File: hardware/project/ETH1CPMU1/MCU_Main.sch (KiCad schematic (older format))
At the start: 31 parts, among them J301 Conn_02x05, J302 Conn_02x01, U301 STM32F765ZGT6, U302 24LC08, Y301 NX3225GD-8MHZ-STD-CRA-3

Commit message: Schematic design
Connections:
- net MAIN_GPIO_OUT1: now reaches U301.22 (PF10,QUADSPI_CLK,DCMI_D11,LCD_DE,EVENTOUT,ADC3_IN8)
- net MAIN_GPIO_OUT2: now reaches U301.26 (PC0,DFSDM1_CKIN0,DFSDM1_DATIN4,SAI2_FS_B,OTG_HS_ULPI_STP,FMC_SDNWE,LCD_R5,EVENTOUT,ADC1_IN10,ADC2_IN10,ADC3_IN10)
- net MAIN_STATUS_IN: now reaches U301.28 (PC2,DFSDM1_CKIN1,SPI2_MISO,DFSDM1_CKOUT,OTG_HS_ULPI_DIR,ETH_MII_TXD2,FMC_SDNE0,EVENTOUT,ADC1_IN12,ADC2_IN12,ADC3_IN12)
- net BASE_GPIO_OUT1: no longer names the net of U301.7 (PC13,EVENTOUT,RTC_TAMP2,RTC_TS,WKUP5)
- net BASE_GPIO_OUT2: no longer names the net of U301.8 (PC14,EVENTOUT,OSC32_IN)
- net BASE_MCLK renamed MAIN_MCLK
- net BASE_MISO renamed MAIN_MISO
- net BASE_MOSI renamed MAIN_MOSI
- net BASE_STATUS_IN: no longer names the net of U301.9 (PC15,EVENTOUT,OSC32_OUT)
- net BASE_~MSS renamed MAIN_~MSS
- net SPI3_MISO: no longer names the net of U301.112 (PC11,DFSDM1_DATIN5,SPI3_MISO,USART3_RX,UART4_RX,QUADSPI_BK2_NCS,SDMMC1_D3,DCMI_D4,EVENTOUT)
- net SPI3_MOSI: no longer names the net of U301.113 (PC12,TRACED3,SPI3_MOSI,I2S3_SD,USART3_CK,UART5_TX,SDMMC1_CK,DCMI_D9,EVENTOUT)
- net SPI3_SCLK: no longer names the net of U301.111 (PC10,DFSDM1_CKIN5,SPI3_SCK,I2S3_CK,USART3_TX,UART4_TX,QUADSPI_BK1_IO1,SDMMC1_D2,DCMI_D8,LCD_R2,EVENTOUT)
- no-connect marks 2 -> 5
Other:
- moved on the sheet: R301, R302, U302
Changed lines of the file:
@@
 $Descr A3 16535 11693
 encoding utf-8
-Sheet 3 12
+Sheet 3 14
 Title ""
 Date ""
@@
 Wire Wire Line
 	14600 2550 14650 2550
-Text Label 2750 6050 0    50   ~ 0
-SPI3_MOSI
-Wire Wire Line
-	3200 6050 2750 6050
-Text Label 2750 5950 0    50   ~ 0
-SPI3_MISO
-Wire Wire Line
-	3200 5950 2750 5950
-Text Label 2750 5850 0    50   ~ 0
-SPI3_SCLK
-Wire Wire Line
-	3200 5850 2750 5850
 Text Label 15050 6550 2    50   ~ 0
 TDO
@@
 L Memory_EEPROM:24LC08 U302
 U 1 1 5E082698
-P 1050 4950
-F 0 "U302" H 1250 5300 50  0000 C CNN
-F 1 "24LC08" H 1250 5200 50  0000 C CNN
-F 2 "" H 1050 4950 50  0001 C CNN
-F 3 "http://ww1.microchip.com/downloads/en/DeviceDoc/21710J.pdf" H 1050 4950 50  0001 C CNN
-	1    1050 4950
+P 1150 7100
+F 0 "U302" H 1350 7450 50  0000 C CNN
+F 1 "24LC08" H 1350 7350 50  0000 C CNN
+F 2 "" H 1150 7100 50  0001 C CNN
+F 3 "http://ww1.microchip.com/downloads/en/DeviceDoc/21710J.pdf" H 1150 7100 50  0001 C CNN
+	1    1150 7100
 	1    0    0    -1
 $EndComp
@@
 L power:+3.3V #PWR0304
 U 1 1 5E08AE5B
-P 1050 4650
-F 0 "#PWR0304" H 1050 4500 50  0001 C CNN
-F 1 "+3.3V" H 1065 4823 50  0000 C CNN
-F 2 "" H 1050 4650 50  0001 C CNN
-F 3 "" H 1050 4650 50  0001 C CNN
-	1    1050 4650
+P 1150 6800
+F 0 "#PWR0304" H 1150 6650 50  0001 C CNN
+F 1 "+3.3V" H 1165 6973 50  0000 C CNN
+F 2 "" H 1150 6800 50  0001 C CNN
+F 3 "" H 1150 6800 50  0001 C CNN
+	1    1150 6800
 	1    0    0    -1
 $EndComp
@@
 L power:GND #PWR0306
 U 1 1 5E08CDE4
-P 1050 5250
-F 0 "#PWR0306" H 1050 5000 50  0001 C CNN
-F 1 "GND" H 1055 5077 50  0000 C CNN
-F 2 "" H 1050 5250 50  0001 C CNN
-F 3 "" H 1050 5250 50  0001 C CNN
-	1    1050 5250
-	1    0    0    -1
-$EndComp
-Wire Wire Line
-	650  4850 600  4850
-Wire Wire Line
-	600  4850 600  4950
-Wire Wire Line
-	600  5050 650  5050
+P 1150 7400
+F 0 "#PWR0306" H 1150 7150 50  0001 C CNN
+F 1 "GND" H 1155 7227 50  0000 C CNN
+F 2 "" H 1150 7400 50  0001 C CNN
+F 3 "" H 1150 7400 50  0001 C CNN
+	1    1150 7400
+	1    0    0    -1
+$EndComp
+Wire Wire Line
+	750  7000 700  7000
+Wire Wire Line
+	700  7000 700  7100
+Wire Wire Line
+	700  7200 750  7200
 $Comp
 L power:GND #PWR0305
 U 1 1 5E096BB8
-P 600 5250
-F 0 "#PWR0305" H 600 5000 50  0001 C CNN
-F 1 "GND" H 605 5077 50  0000 C CNN
-F 2 "" H 600 5250 50  0001 C CNN
-F 3 "" H 600 5250 50  0001 C CNN
-	1    600  5250
-	1    0    0    -1
-$EndComp
-Wire Wire Line
-	600  5250 600  5050
-Connection ~ 600  5050
-Wire Wire Line
-	650  4950 600  4950
-Connection ~ 600  4950
-Wire Wire Line
-	600  4950 600  5050
-Wire Wire Line
-	1450 5050 1950 5050
-Text Label 1950 5050 2    50   ~ 0
+P 700 7400
+F 0 "#PWR0305" H 700 7150 50  0001 C CNN
+F 1 "GND" H 705 7227 50  0000 C CNN
+F 2 "" H 700 7400 50  0001 C CNN
+F 3 "" H 700 7400 50  0001 C CNN
+	1    700  7400
+	1    0    0    -1
+$EndComp
+Wire Wire Line
+	700  7400 700  7200
+Connection ~ 700  7200
+Wire Wire Line
+	750  7100 700  7100
+Connection ~ 700  7100
+Wire Wire Line
+	700  7100 700  7200
+Wire Wire Line
+	1550 7200 2050 7200
+Text Label 2050 7200 2    50   ~ 0
 EEPROM_WP
-Text Label 1950 4950 2    50   ~ 0
+Text Label 2050 7100 2    50   ~ 0
 EEPROM_SCL
-Text Label 1950 4850 2    50   ~ 0
+Text Label 2050 7000 2    50   ~ 0
 EEPROM_SDA
 $Comp
 L Device:R R301
 U 1 1 5E0F3906
-P 2000 4650
-F 0 "R301" H 2070 4696 50  0000 L CNN
-F 1 "4k7" H 2070 4605 50  0000 L CNN
-F 2 "Resistor_SMD:R_0603_1608Metric_Pad1.05x0.95mm_HandSolder" V 1930 4650 50  0001 C CNN
-F 3 "~" H 2000 4650 50  0001 C CNN
-	1    2000 4650
+P 2100 6800
+F 0 "R301" H 2170 6846 50  0000 L CNN
+F 1 "4k7" H 2170 6755 50  0000 L CNN
+F 2 "Resistor_SMD:R_0603_1608Metric_Pad1.05x0.95mm_HandSolder" V 2030 6800 50  0001 C CNN
+F 3 "~" H 2100 6800 50  0001 C CNN
+	1    2100 6800
 	1    0    0    -1
 $EndComp
@@
 L Device:R R302
 U 1 1 5E0F3C03
-P 2350 4650
-F 0 "R302" H 2420 4696 50  0000 L CNN
-F 1 "4k7" H 2420 4605 50  0000 L CNN
-F 2 "Resistor_SMD:R_0603_1608Metric_Pad1.05x0.95mm_HandSolder" V 2280 4650 50  0001 C CNN
-F 3 "~" H 2350 4650 50  0001 C CNN
-	1    2350 4650
-	1    0    0    -1
-$EndComp
-Wire Wire Line
-	2000 4850 2000 4800
-Wire Wire Line
-	1450 4850 2000 4850
-Wire Wire Line
-	2350 4950 2350 4800
-Wire Wire Line
-	1450 4950 2350 4950
-Wire Wire Line
-	2000 4500 2000 4450
-Wire Wire Line
-	2000 4450 2350 4450
-Wire Wire Line
-	2350 4450 2350 4500
+P 2450 6800
+F 0 "R302" H 2520 6846 50  0000 L CNN
+F 1 "4k7" H 2520 6755 50  0000 L CNN
+F 2 "Resistor_SMD:R_0603_1608Metric_Pad1.05x0.95mm_HandSolder" V 2380 6800 50  0001 C CNN
+F 3 "~" H 2450 6800 50  0001 C CNN
+	1    2450 6800
+	1    0    0    -1
+$EndComp
+Wire Wire Line
+	2100 7000 2100 6950
+Wire Wire Line
+	1550 7000 2100 7000
+Wire Wire Line
+	2450 7100 2450 6950
+Wire Wire Line
+	1550 7100 2450 7100
+Wire Wire Line
+	2100 6650 2100 6600
+Wire Wire Line
+	2100 6600 2450 6600
+Wire Wire Line
+	2450 6600 2450 6650
 $Comp
 L power:+3.3V #PWR0303
 U 1 1 5E117FC1
-P 2350 4400
-F 0 "#PWR0303" H 2350 4250 50  0001 C CNN
-F 1 "+3.3V" H 2365 4573 50  0000 C CNN
-F 2 "" H 2350 4400 50  0001 C CNN
-F 3 "" H 2350 4400 50  0001 C CNN
-	1    2350 4400
-	1    0    0    -1
-$EndComp
-Wire Wire Line
-	2350 4400 2350 4450
-Connection ~ 2350 4450
+P 2450 6550
+F 0 "#PWR0303" H 2450 6400 50  0001 C CNN
+F 1 "+3.3V" H 2465 6723 50  0000 C CNN
+F 2 "" H 2450 6550 50  0001 C CNN
+F 3 "" H 2450 6550 50  0001 C CNN
+	1    2450 6550
+	1    0    0    -1
+$EndComp
+Wire Wire Line
+	2450 6550 2450 6600
+Connection ~ 2450 6600
 Wire Wire Line
 	3200 2750 2700 2750
@@
 Wire Wire Line
 	700  9650 700  9550
-Text HLabel 3150 2150 0    50   Output ~ 0
-BASE_MCLK
-Text HLabel 3150 2350 0    50   Output ~ 0
-BASE_MOSI
-Text HLabel 3150 2250 0    50   Input ~ 0
-BASE_MISO
-Text HLabel 3150 2050 0    50   Output ~ 0
-BASE_~MSS
-Wire Wire Line
-	3150 2350 3200 2350
-Wire Wire Line
-	3200 2250 3150 2250
-Wire Wire Line
-	3150 2150 3200 2150
-Wire Wire Line
-	3200 2050 3150 2050
 Text HLabel 14650 7550 2    50   Output ~ 0
 TRIG_EN
@@
 Wire Wire Line
 	14600 7750 14650 7750
-Text HLabel 3150 6350 0    50   Input ~ 0
-BASE_STATUS_IN
-Text HLabel 3150 6250 0    50   Output ~ 0
-BASE_GPIO_OUT2
-Text HLabel 3150 6150 0    50   Output ~ 0
-BASE_GPIO_OUT1
-Wire Wire Line
-	3150 6150 3200 6150
-Wire Wire Line
-	3200 6250 3150 6250
-Wire Wire Line
-	3150 6350 3200 6350
+Text HLabel 3150 5050 0    50   Input ~ 0
+MAIN_STATUS_IN
+Text HLabel 3150 4850 0    50   Output ~ 0
+MAIN_GPIO_OUT2
+Text HLabel 3150 2450 0    50   Output ~ 0
+MAIN_GPIO_OUT1
+Wire Wire Line
+	3150 2450 3200 2450
+Wire Wire Line
+	3200 4850 3150 4850
+Wire Wire Line
+	3150 5050 3200 5050
+Wire Wire Line
+	3200 2050 3150 2050
+Wire Wire Line
+	3150 2150 3200 2150
+Wire Wire Line
+	3200 2250 3150 2250
+Wire Wire Line
+	3150 2350 3200 2350
+Text HLabel 3150 2050 0    50   Output ~ 0
+MAIN_~MSS
+Text HLabel 3150 2250 0    50   Input ~ 0
+MAIN_MISO
+Text HLabel 3150 2350 0    50   Output ~ 0
+MAIN_MOSI
+Text HLabel 3150 2150 0    50   Output ~ 0
+MAIN_MCLK
+NoConn ~ 3200 5850
+NoConn ~ 3200 5950
+NoConn ~ 3200 6050
 $EndSCHEMATC

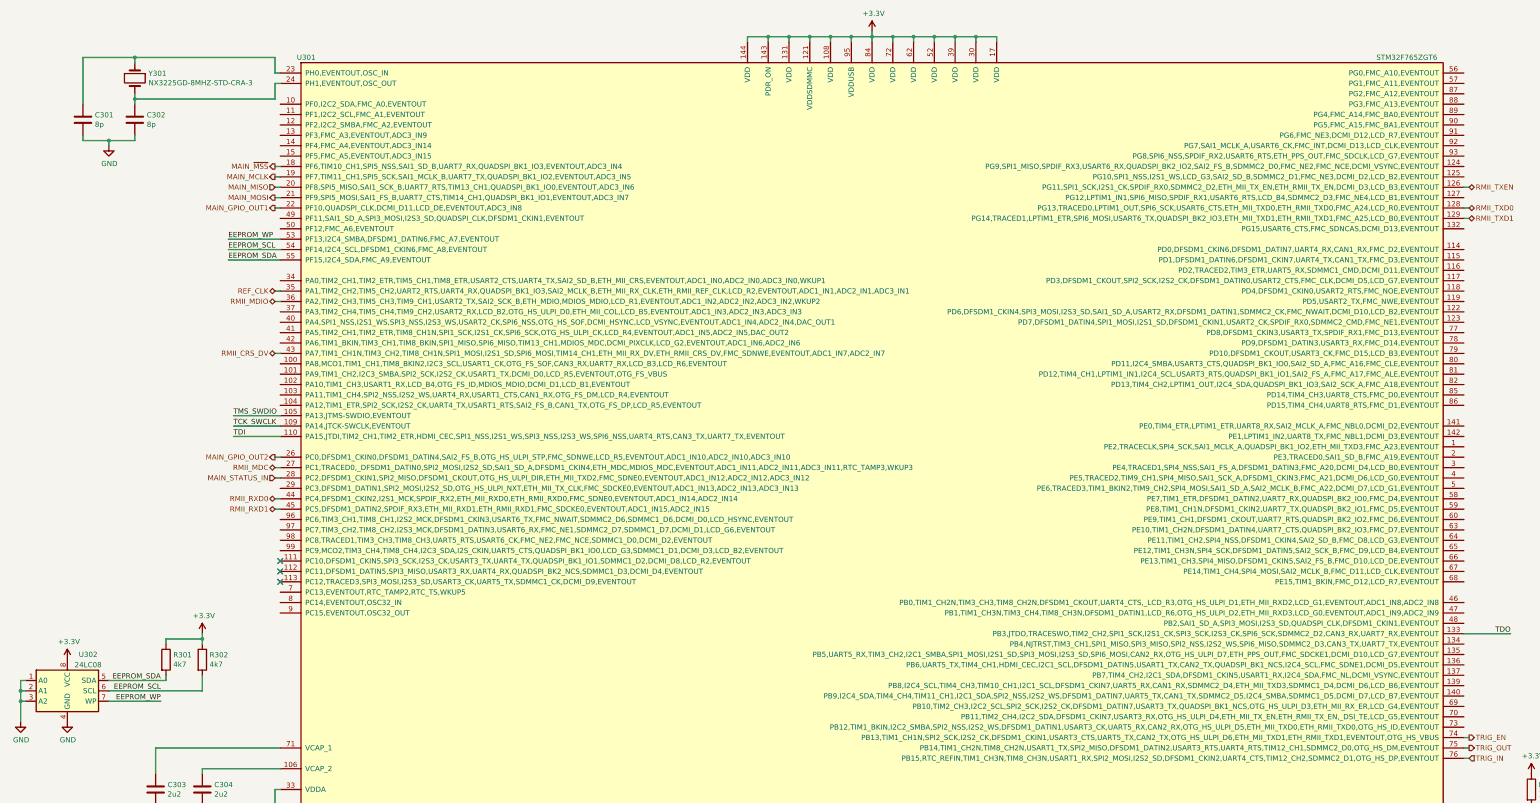
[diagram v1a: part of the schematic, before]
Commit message: Function generator schematic design.
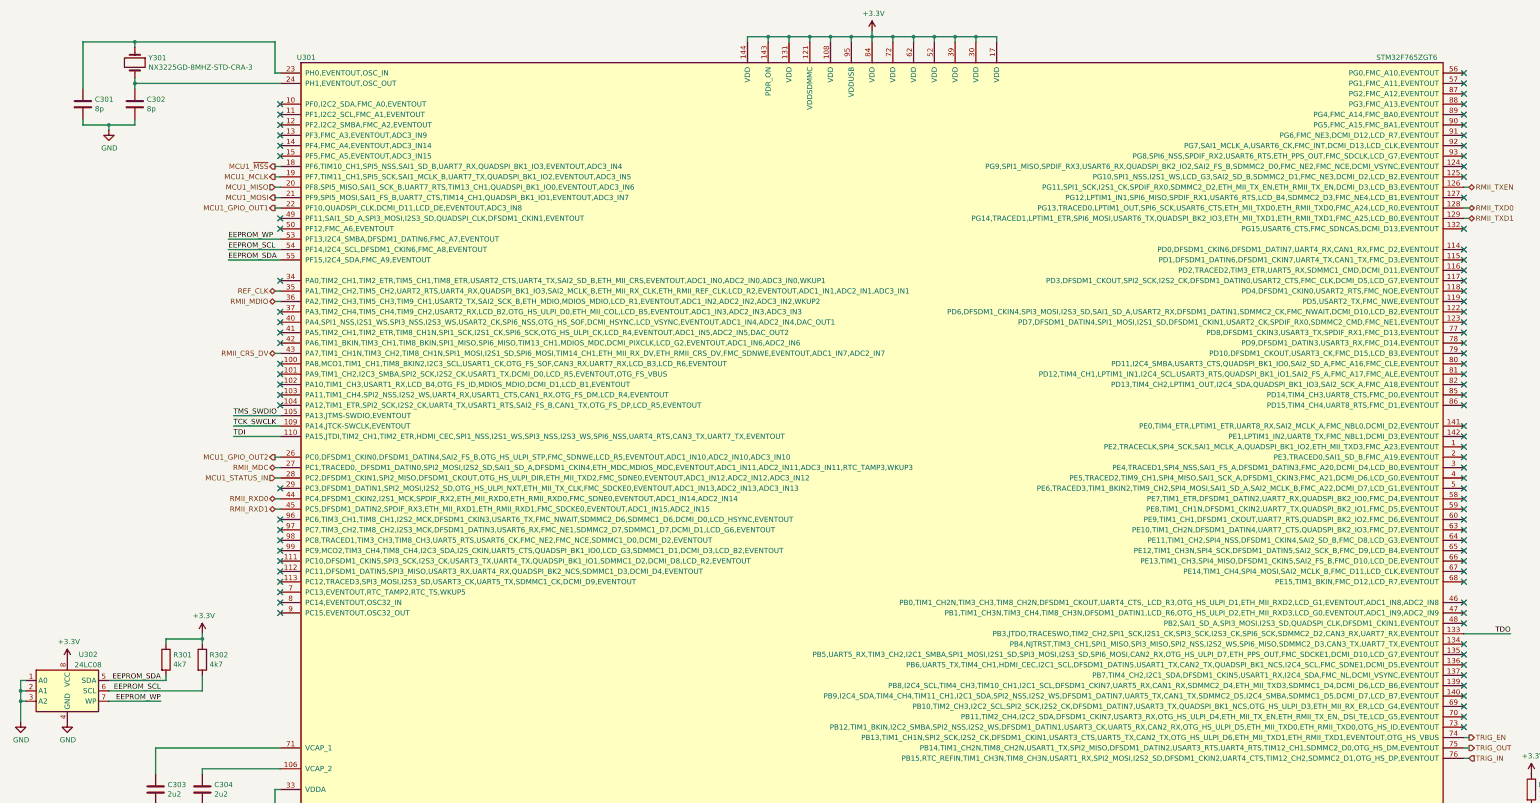
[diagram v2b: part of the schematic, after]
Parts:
- C303, C304: footprint (none) -> Capacitor_SMD:C_0805_2012Metric_Pad1.15x1.40mm_HandSolder
- C306, C320: footprint (none) -> Capacitor_SMD:C_0603_1608Metric_Pad1.05x0.95mm_HandSolder
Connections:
- net MAIN_GPIO_OUT1 renamed MCU1_GPIO_OUT1
- net MAIN_GPIO_OUT2 renamed MCU1_GPIO_OUT2
- net MAIN_MCLK renamed MCU1_MCLK
- net MAIN_MISO renamed MCU1_MISO
- net MAIN_MOSI renamed MCU1_MOSI
- net MAIN_STATUS_IN renamed MCU1_STATUS_IN
- net MAIN_~MSS renamed MCU1_~MSS
- no-connect marks 5 -> 88
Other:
- moved on the sheet: C301, C302, Y301
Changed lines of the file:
@@
 $Descr A3 16535 11693
 encoding utf-8
-Sheet 3 14
+Sheet 3 15
 Title ""
 Date ""
@@
 F 0 "C306" H 3265 8946 50  0000 L CNN
 F 1 "1u" H 3265 8855 50  0000 L CNN
-F 2 "" H 3188 8750 50  0001 C CNN
+F 2 "Capacitor_SMD:C_0603_1608Metric_Pad1.05x0.95mm_HandSolder" H 3188 8750 50  0001 C CNN
 F 3 "~" H 3150 8900 50  0001 C CNN
 	1    3150 8900
@@
 F 0 "C320" H 7365 10746 50  0000 L CNN
 F 1 "1u" H 7365 10655 50  0000 L CNN
-F 2 "" H 7288 10550 50  0001 C CNN
+F 2 "Capacitor_SMD:C_0603_1608Metric_Pad1.05x0.95mm_HandSolder" H 7288 10550 50  0001 C CNN
 F 3 "~" H 7250 10700 50  0001 C CNN
 	1    7250 10700
@@
 F 0 "C304" H 2565 8096 50  0000 L CNN
 F 1 "2u2" H 2565 8005 50  0000 L CNN
-F 2 "" H 2488 7900 50  0001 C CNN
+F 2 "Capacitor_SMD:C_0805_2012Metric_Pad1.15x1.40mm_HandSolder" H 2488 7900 50  0001 C CNN
 F 3 "~" H 2450 8050 50  0001 C CNN
 	1    2450 8050
@@
 F 0 "C303" H 2115 8096 50  0000 L CNN
 F 1 "2u2" H 2115 8005 50  0000 L CNN
-F 2 "" H 2038 7900 50  0001 C CNN
+F 2 "Capacitor_SMD:C_0805_2012Metric_Pad1.15x1.40mm_HandSolder" H 2038 7900 50  0001 C CNN
 F 3 "~" H 2000 8050 50  0001 C CNN
 	1    2000 8050
@@
 L Device:Crystal Y301
 U 1 1 5DBCE9A3
-P 1800 1200
-F 0 "Y301" V 1754 1331 50  0000 L CNN
-F 1 "NX3225GD-8MHZ-STD-CRA-3" V 1845 1331 50  0000 L CNN
-F 2 "" H 1800 1200 50  0001 C CNN
-F 3 "~" H 1800 1200 50  0001 C CNN
-	1    1800 1200
+P 1800 1050
+F 0 "Y301" V 1754 1181 50  0000 L CNN
+F 1 "NX3225GD-8MHZ-STD-CRA-3" V 1845 1181 50  0000 L CNN
+F 2 "" H 1800 1050 50  0001 C CNN
+F 3 "~" H 1800 1050 50  0001 C CNN
+	1    1800 1050
 	0    1    1    0
 $EndComp
 Wire Wire Line
-	3200 1250 3150 1250
-Wire Wire Line
-	3150 1250 3150 1400
-Wire Wire Line
-	3150 1400 1800 1400
-Wire Wire Line
-	1800 1400 1800 1350
-Wire Wire Line
-	1800 1050 1800 1000
-Wire Wire Line
-	1800 1000 3150 1000
-Wire Wire Line
-	3150 1000 3150 1150
+	1800 1250 1800 1200
+Wire Wire Line
+	1800 900  1800 850
+Wire Wire Line
+	1800 850  3150 850
+Wire Wire Line
+	3150 850  3150 1150
 Wire Wire Line
 	3150 1150 3200 1150
@@
 L Device:C C302
 U 1 1 5DBE0849
-P 1800 1600
-F 0 "C302" H 1915 1646 50  0000 L CNN
-F 1 "8p" H 1915 1555 50  0000 L CNN
-F 2 "Capacitor_SMD:C_0603_1608Metric_Pad1.05x0.95mm_HandSolder" H 1838 1450 50  0001 C CNN
-F 3 "~" H 1800 1600 50  0001 C CNN
-	1    1800 1600
+P 1800 1450
+F 0 "C302" H 1915 1496 50  0000 L CNN
+F 1 "8p" H 1915 1405 50  0000 L CNN
+F 2 "Capacitor_SMD:C_0603_1608Metric_Pad1.05x0.95mm_HandSolder" H 1838 1300 50  0001 C CNN
+F 3 "~" H 1800 1450 50  0001 C CNN
+	1    1800 1450
 	1    0    0    -1
 $EndComp
@@
 L Device:C C301
 U 1 1 5DBE0C2D
-P 1300 1600
-F 0 "C301" H 1415 1646 50  0000 L CNN
-F 1 "8p" H 1415 1555 50  0000 L CNN
-F 2 "Capacitor_SMD:C_0603_1608Metric_Pad1.05x0.95mm_HandSolder" H 1338 1450 50  0001 C CNN
-F 3 "~" H 1300 1600 50  0001 C CNN
-	1    1300 1600
-	1    0    0    -1
-$EndComp
-Wire Wire Line
-	1800 1450 1800 1400
-Connection ~ 1800 1400
-Wire Wire Line
-	1800 1000 1300 1000
-Wire Wire Line
-	1300 1000 1300 1450
-Connection ~ 1800 1000
-Wire Wire Line
-	1300 1750 1300 1800
-Wire Wire Line
-	1300 1800 1550 1800
-Wire Wire Line
-	1800 1800 1800 1750
+P 1300 1450
+F 0 "C301" H 1415 1496 50  0000 L CNN
+F 1 "8p" H 1415 1405 50  0000 L CNN
+F 2 "Capacitor_SMD:C_0603_1608Metric_Pad1.05x0.95mm_HandSolder" H 1338 1300 50  0001 C CNN
+F 3 "~" H 1300 1450 50  0001 C CNN
+	1    1300 1450
+	1    0    0    -1
+$EndComp
+Wire Wire Line
+	1800 1300 1800 1250
+Connection ~ 1800 1250
+Wire Wire Line
+	1800 850  1300 850
+Wire Wire Line
+	1300 850  1300 1300
+Connection ~ 1800 850
+Wire Wire Line
+	1300 1600 1300 1650
+Wire Wire Line
+	1300 1650 1550 1650
+Wire Wire Line
+	1800 1650 1800 1600
 $Comp
 L power:GND #PWR0302
 U 1 1 5DC11C96
-P 1550 1850
-F 0 "#PWR0302" H 1550 1600 50  0001 C CNN
-F 1 "GND" H 1555 1677 50  0000 C CNN
-F 2 "" H 1550 1850 50  0001 C CNN
-F 3 "" H 1550 1850 50  0001 C CNN
-	1    1550 1850
-	1    0    0    -1
-$EndComp
-Wire Wire Line
-	1550 1850 1550 1800
-Connection ~ 1550 1800
-Wire Wire Line
-	1550 1800 1800 1800
+P 1550 1700
+F 0 "#PWR0302" H 1550 1450 50  0001 C CNN
+F 1 "GND" H 1555 1527 50  0000 C CNN
+F 2 "" H 1550 1700 50  0001 C CNN
+F 3 "" H 1550 1700 50  0001 C CNN
+	1    1550 1700
+	1    0    0    -1
+$EndComp
+Wire Wire Line
+	1550 1700 1550 1650
+Connection ~ 1550 1650
+Wire Wire Line
+	1550 1650 1800 1650
 Wire Wire Line
 	3200 4450 2750 4450
@@
 	14600 7750 14650 7750
 Text HLabel 3150 5050 0    50   Input ~ 0
-MAIN_STATUS_IN
+MCU1_STATUS_IN
 Text HLabel 3150 4850 0    50   Output ~ 0
-MAIN_GPIO_OUT2
+MCU1_GPIO_OUT2
 Text HLabel 3150 2450 0    50   Output ~ 0
-MAIN_GPIO_OUT1
+MCU1_GPIO_OUT1
 Wire Wire Line
 	3150 2450 3200 2450
@@
 	3150 2350 3200 2350
 Text HLabel 3150 2050 0    50   Output ~ 0
-MAIN_~MSS
+MCU1_~MSS
 Text HLabel 3150 2250 0    50   Input ~ 0
-MAIN_MISO
+MCU1_MISO
 Text HLabel 3150 2350 0    50   Output ~ 0
-MAIN_MOSI
+MCU1_MOSI
 Text HLabel 3150 2150 0    50   Output ~ 0
-MAIN_MCLK
+MCU1_MCLK
 NoConn ~ 3200 5850
 NoConn ~ 3200 5950
 NoConn ~ 3200 6050
+Wire Wire Line
+	1800 1250 3200 1250
+NoConn ~ 3200 1750
+NoConn ~ 3200 1850
+NoConn ~ 3200 1950
+NoConn ~ 3200 2550
+NoConn ~ 3200 2650
+NoConn ~ 3200 3150
+NoConn ~ 3200 1450
+NoConn ~ 3200 1550
+NoConn ~ 3200 1650
+NoConn ~ 3200 3450
+NoConn ~ 3200 3550
+NoConn ~ 3200 3650
+NoConn ~ 3200 3750
+NoConn ~ 3200 3950
+NoConn ~ 3200 4050
+NoConn ~ 3200 4150
+NoConn ~ 3200 4250
+NoConn ~ 3200 4350
+NoConn ~ 3200 5150
+NoConn ~ 3200 5450
+NoConn ~ 3200 5550
+NoConn ~ 3200 5650
+NoConn ~ 3200 5750
+NoConn ~ 3200 6150
+NoConn ~ 3200 6250
+NoConn ~ 3200 6350
+NoConn ~ 14600 1150
+NoConn ~ 14600 1250
+NoConn ~ 14600 1350
+NoConn ~ 14600 1450
+NoConn ~ 14600 1550
+NoConn ~ 14600 1650
+NoConn ~ 14600 1750
+NoConn ~ 14600 1850
+NoConn ~ 14600 1950
+NoConn ~ 14600 2050
+NoConn ~ 14600 2150
+NoConn ~ 14600 2350
+NoConn ~ 14600 2650
+NoConn ~ 14600 2850
+NoConn ~ 14600 2950
+NoConn ~ 14600 3050
+NoConn ~ 14600 3150
+NoConn ~ 14600 3250
+NoConn ~ 14600 3350
+NoConn ~ 14600 3450
+NoConn ~ 14600 3550
+NoConn ~ 14600 3650
+NoConn ~ 14600 3750
+NoConn ~ 14600 3850
+NoConn ~ 14600 3950
+NoConn ~ 14600 4050
+NoConn ~ 14600 4150
+NoConn ~ 14600 4250
+NoConn ~ 14600 4350
+NoConn ~ 14600 4550
+NoConn ~ 14600 4650
+NoConn ~ 14600 4750
+NoConn ~ 14600 4850
+NoConn ~ 14600 4950
+NoConn ~ 14600 5050
+NoConn ~ 14600 5150
+NoConn ~ 14600 5250
+NoConn ~ 14600 5350
+NoConn ~ 14600 5450
+NoConn ~ 14600 5550
+NoConn ~ 14600 5650
+NoConn ~ 14600 5750
+NoConn ~ 14600 5850
+NoConn ~ 14600 5950
+NoConn ~ 14600 6050
+NoConn ~ 14600 6250
+NoConn ~ 14600 6350
+NoConn ~ 14600 6450
+NoConn ~ 14600 6650
+NoConn ~ 14600 6750
+NoConn ~ 14600 6850
+NoConn ~ 14600 6950
+NoConn ~ 14600 7050
+NoConn ~ 14600 7150
+NoConn ~ 14600 7250
+NoConn ~ 14600 7350
+NoConn ~ 14600 7450
 $EndSCHEMATC

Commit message: New footprint development, changes in schematics.
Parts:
- FB301: footprint Resistor_SMD:R_0805_2012Metric_Pad1.15x1.40mm_HandSolder -> Inductor_SMD:L_0805_2012Metric_Pad1.15x1.40mm_HandSolder
- J301: footprint (none) -> Connector_PinHeader_1.27mm:PinHeader_2x05_P1.27mm_Vertical
- J302: footprint (none) -> Connector_PinHeader_2.54mm:PinHeader_1x02_P2.54mm_Vertical
- Y301: footprint (none) -> ETH1CPMU1:NX3225GD
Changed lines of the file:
@@
 F 0 "J301" H 9900 10867 50  0000 C CNN
 F 1 "Conn_02x05" H 9900 10776 50  0000 C CNN
-F 2 "" H 9850 10450 50  0001 C CNN
+F 2 "Connector_PinHeader_1.27mm:PinHeader_2x05_P1.27mm_Vertical" H 9850 10450 50  0001 C CNN
 F 3 "~" H 9850 10450 50  0001 C CNN
 	1    9850 10450
@@
 F 0 "FB301" V 6726 10500 50  0000 C CNN
 F 1 "742792031" V 6817 10500 50  0000 C CNN
-F 2 "Resistor_SMD:R_0805_2012Metric_Pad1.15x1.40mm_HandSolder" V 6930 10500 50  0001 C CNN
+F 2 "Inductor_SMD:L_0805_2012Metric_Pad1.15x1.40mm_HandSolder" V 6930 10500 50  0001 C CNN
 F 3 "~" H 7000 10500 50  0001 C CNN
 	1    7000 10500
@@
 F 0 "J302" V 8054 10730 50  0000 L CNN
 F 1 "Conn_02x01" V 8145 10730 50  0000 L CNN
-F 2 "" H 8050 10650 50  0001 C CNN
+F 2 "Connector_PinHeader_2.54mm:PinHeader_1x02_P2.54mm_Vertical" H 8050 10650 50  0001 C CNN
 F 3 "~" H 8050 10650 50  0001 C CNN
 	1    8050 10650
@@
 F 0 "Y301" V 1754 1181 50  0000 L CNN
 F 1 "NX3225GD-8MHZ-STD-CRA-3" V 1845 1181 50  0000 L CNN
-F 2 "" H 1800 1050 50  0001 C CNN
+F 2 "ETH1CPMU1:NX3225GD" H 1800 1050 50  0001 C CNN
 F 3 "~" H 1800 1050 50  0001 C CNN
 	1    1800 1050

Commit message: Schematic and PCB design.
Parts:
- U302: value 24LC08 -> 24LC08B-E/MS; footprint (none) -> Package_SO:MSOP-8_3x3mm_P0.65mm
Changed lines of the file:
@@
 U 1 1 5E082698
 P 1150 7100
-F 0 "U302" H 1350 7450 50  0000 C CNN
-F 1 "24LC08" H 1350 7350 50  0000 C CNN
-F 2 "" H 1150 7100 50  0001 C CNN
+F 0 "U302" H 1500 7450 50  0000 C CNN
+F 1 "24LC08B-E/MS" H 1500 7350 50  0000 C CNN
+F 2 "Package_SO:MSOP-8_3x3mm_P0.65mm" H 1150 7100 50  0001 C CNN
 F 3 "http://ww1.microchip.com/downloads/en/DeviceDoc/21710J.pdf" H 1150 7100 50  0001 C CNN
 	1    1150 7100
